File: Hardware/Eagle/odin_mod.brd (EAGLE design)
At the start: 21.4 x 22.8 mm, 44 parts, among them Q1 IRLML0030, Q2 IRLML0030, Q3 IRLML0030, Q4 IRLML0030

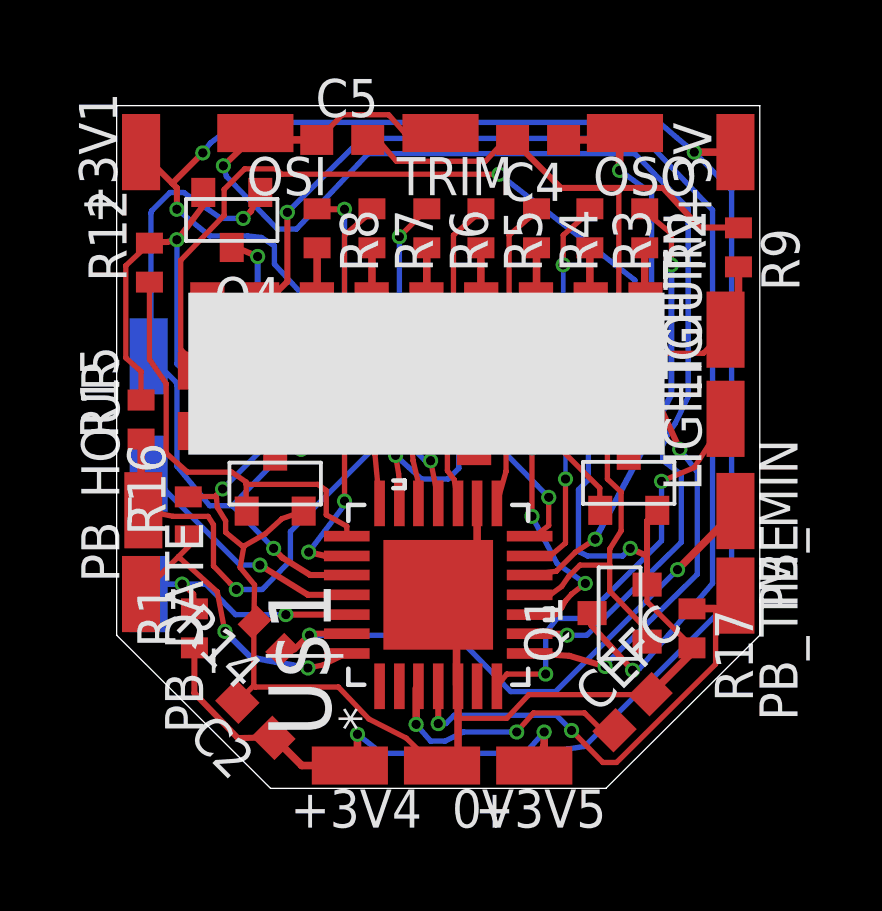
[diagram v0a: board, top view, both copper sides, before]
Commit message: Lowered segment resistors and optimized traces.
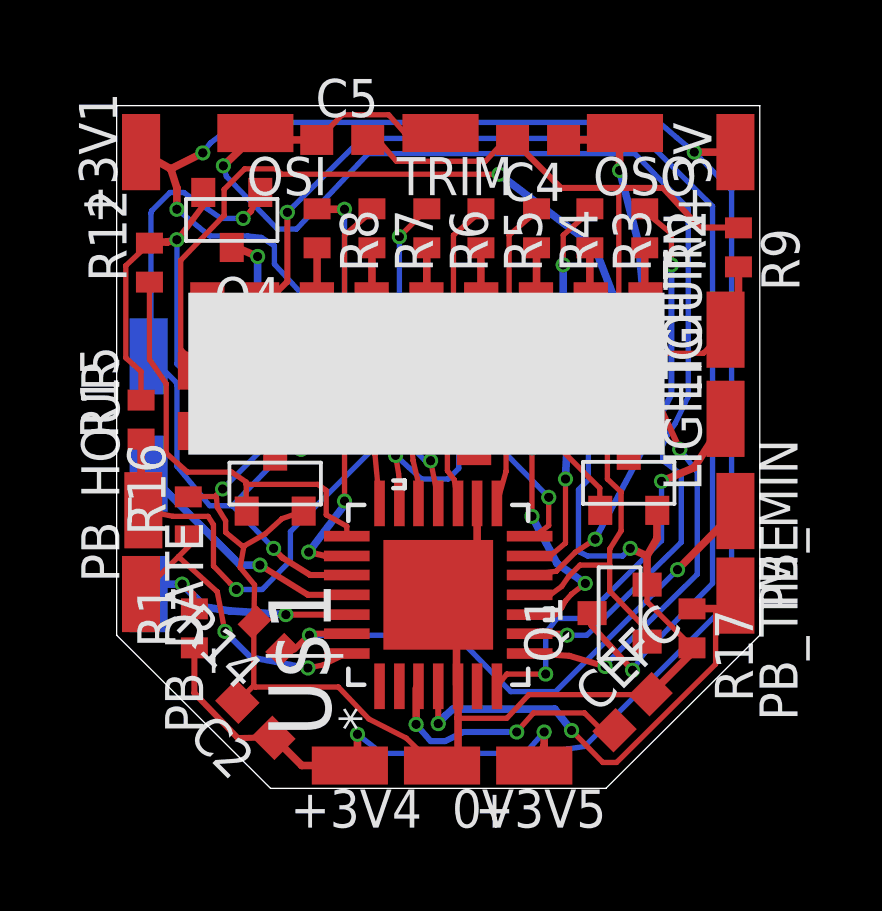
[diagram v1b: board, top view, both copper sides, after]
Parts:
- R2, R3, R4, R5, R6, R7, R8: value 82 -> 75

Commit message: Optimized ODIN II layout by means of having more space to solder the two transistors below the display.
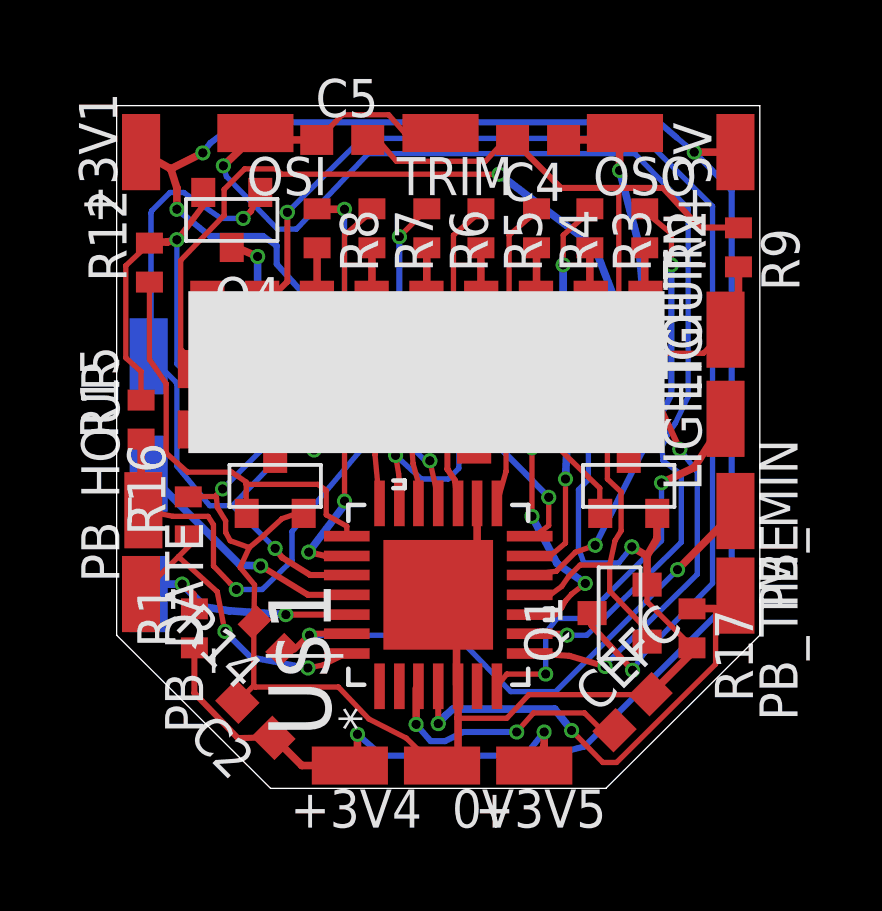
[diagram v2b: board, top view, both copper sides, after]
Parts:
- moved Q3 0.10 mm to (17.0, 10.1)
- moved Q2 0.08 mm to (5.23, 10.1)
- moved U$3 0.05 mm to (2.34, 11.2)
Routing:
- net GND: track 96.7 -> 97.3 mm

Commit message: Increased trace with of some connections.
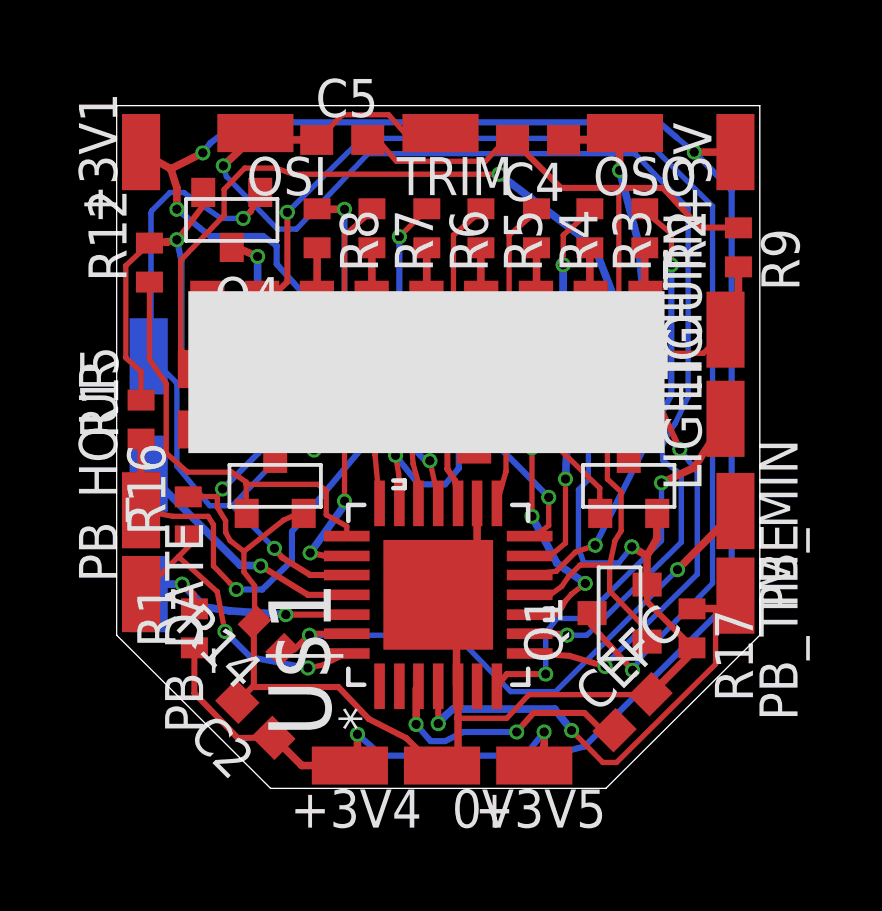
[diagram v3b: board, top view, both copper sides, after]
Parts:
- moved PB_HOUR 0.08 mm to (0.76, 9.27)
